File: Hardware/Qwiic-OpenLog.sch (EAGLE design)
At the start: 40 parts, among them J1 MICRO-SD, J10 GATORGATOR_MINI, J2 GATORGATOR_MINI, J3 GATORGATOR_MINI, J4 GATORGATOR_MINI, J5 ISP, J6 GATORGATOR_MINI, J7 GATORGATOR_MINI, J8 GATORGATOR_MINI, J9 GATORGATOR_MINI, Q1 16MHZ, U1 RV-1805, U2 ATMEGA328P

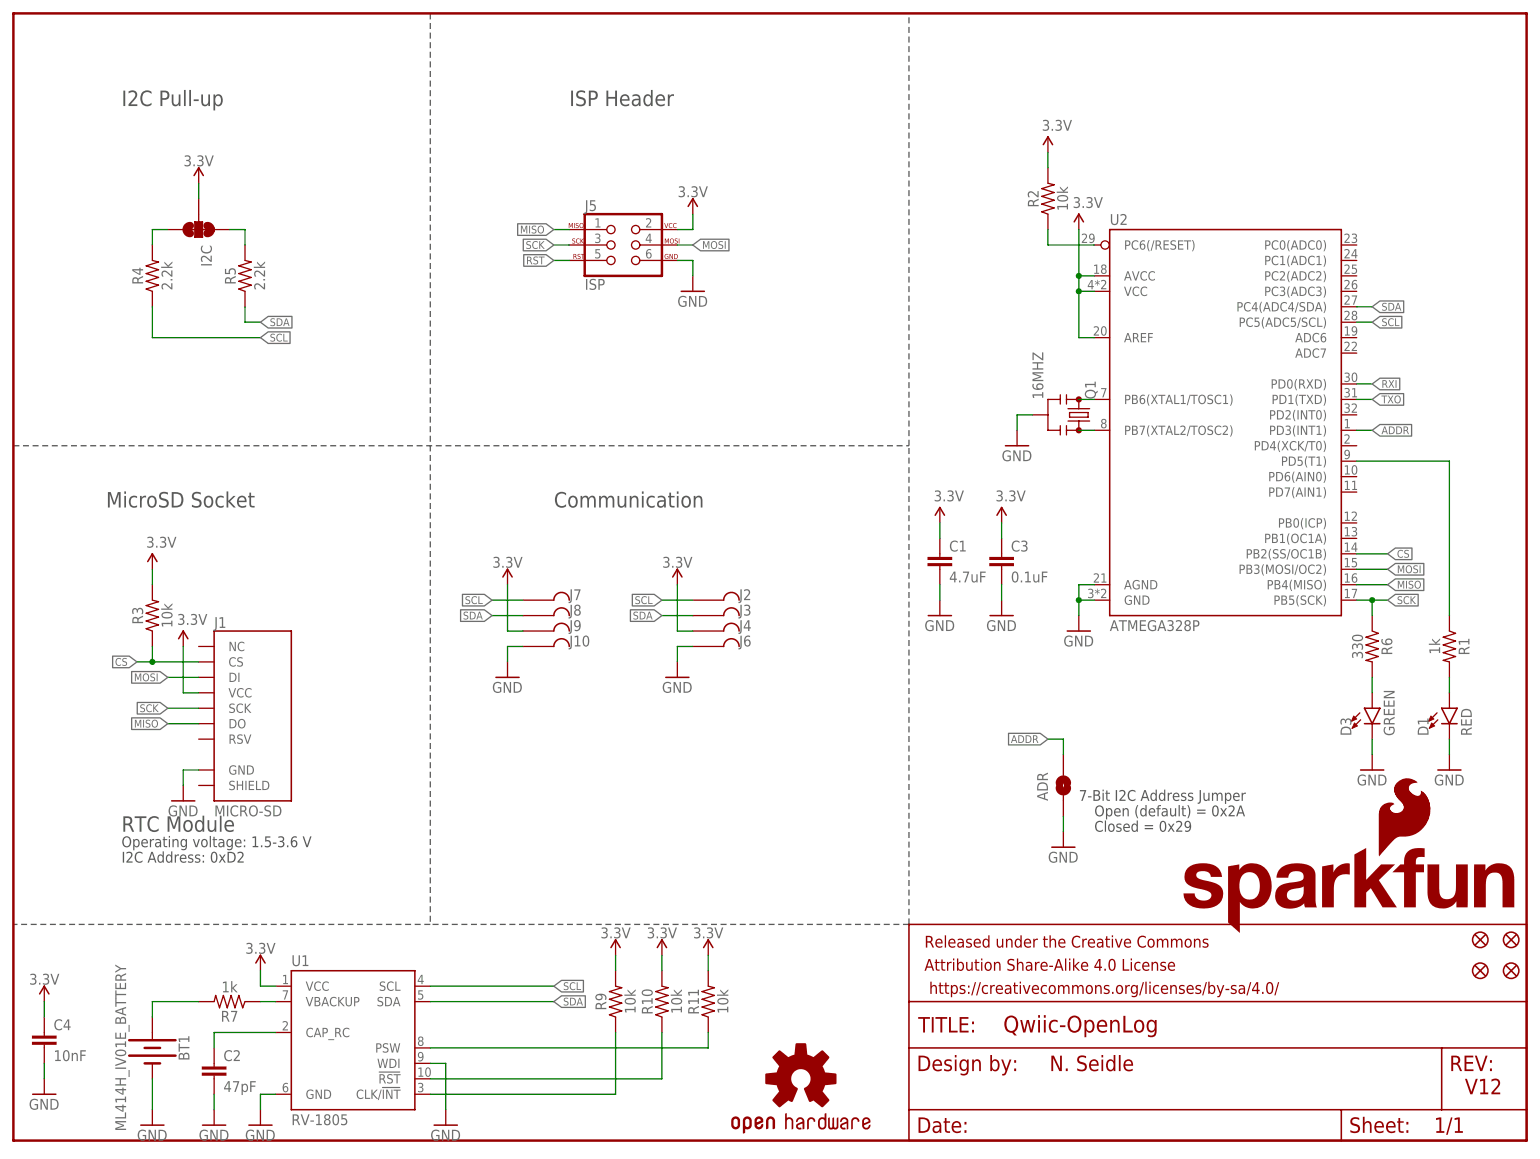
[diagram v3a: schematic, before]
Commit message: updating silk
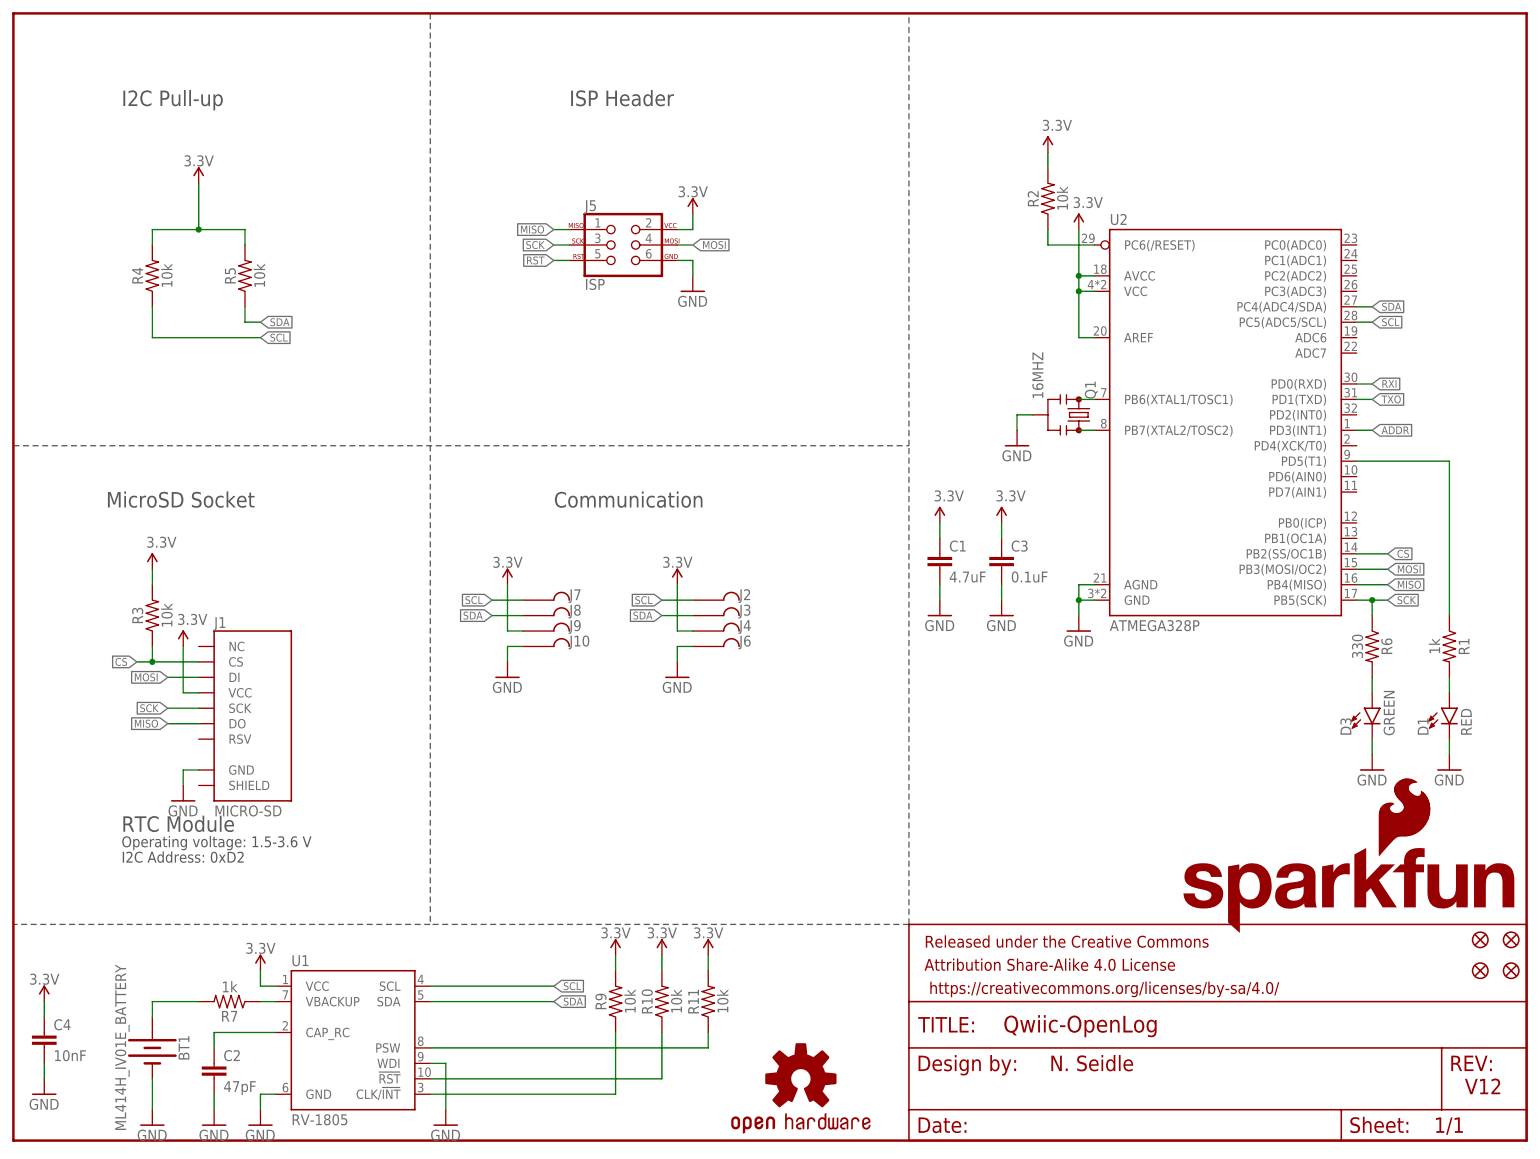
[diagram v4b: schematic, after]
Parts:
- removed ADR: SOLDERJUMPERNO, SparkFun:SOLDERJUMPERNO
- removed I2C: JUMPER-SMT_3_2-NC_TRACE_SILK, SparkFun-Jumpers:JUMPER-SMT_3_2-NC_TRACE_SILK
- R4, R5: value 2.2k -> 10k; device SparkFun-Resistors:2.2KOHM-0603-1/10W-1% -> SparkFun-Resistors:10KOHM-0603-1/10W-1%
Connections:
- removed net N$5: I2C.1, R5.2
- removed net N$6: I2C.3, R4.2
- net 3.3V: now also R4.2, R5.2; no longer I2C.2
- net ADDR: no longer ADR.2
- net GND: no longer ADR.1
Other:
- note removed: "7-Bit I2C Address Jumper"
- note removed: "Closed = 0x29"
- note removed: "Open (default) = 0x2A"
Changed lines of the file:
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@@
 <?xml version="1.0" encoding="utf-8"?>
 <!DOCTYPE eagle SYSTEM "eagle.dtd">
-<eagle version="9.3.1">
+<eagle version="9.1.0">
 <drawing>
 <settings>
@@
 <part name="P+3" library="SparkFun" deviceset="3.3V" device=""/>
 <part name="GND7" library="SparkFun" deviceset="GND" device=""/>
-<part name="GND10" library="SparkFun" deviceset="GND" device=""/>
-<part name="ADR" library="SparkFun" deviceset="SOLDERJUMPER" device="NO" value=""/>
-<part name="R4" library="SparkFun-Resistors" deviceset="2.2KOHM" device="-0603-1/10W-1%" value="2.2k"/>
-<part name="R5" library="SparkFun-Resistors" deviceset="2.2KOHM" device="-0603-1/10W-1%" value="2.2k"/>
-<part name="I2C" library="SparkFun-Jumpers" deviceset="JUMPER-SMT_3_2-NC_TRACE" device="_SILK" value=""/>
+<part name="R4" library="SparkFun-Resistors" deviceset="10KOHM" device="-0603-1/10W-1%" value="10k"/>
+<part name="R5" library="SparkFun-Resistors" deviceset="10KOHM" device="-0603-1/10W-1%" value="10k"/>
 <part name="SUPPLY1" library="SparkFun-PowerSymbols" deviceset="3.3V" device=""/>
 <part name="J5" library="SparkFun-Connectors" deviceset="AVR_SPI_PROG_3X2" device="TESTPOINTS" value="ISP"/>
@@
 <wire x1="0" y1="114.3" x2="147.32" y2="114.3" width="0.2032" layer="97" style="shortdash"/>
 <wire x1="68.58" y1="185.42" x2="68.58" y2="35.56" width="0.2032" layer="97" style="shortdash"/>
-<text x="175.26" y="55.88" size="1.778" layer="97">7-Bit I2C Address Jumper</text>
-<text x="177.8" y="50.8" size="1.778" layer="97">Closed = 0x29</text>
-<text x="177.8" y="53.34" size="1.778" layer="97">Open (default) = 0x2A</text>
 <text x="17.78" y="50.8" size="2.54" layer="97" font="vector">RTC Module</text>
 <text x="17.78" y="48.26" size="1.778" layer="97">Operating voltage: 1.5-3.6 V</text>
@@
 <attribute name="VALUE" x="149.86" y="83.82" size="1.778" layer="96"/>
 </instance>
-<instance part="GND10" gate="1" x="172.72" y="48.26" smashed="yes">
-<attribute name="VALUE" x="170.18" y="45.72" size="1.778" layer="96"/>
-</instance>
-<instance part="ADR" gate="1" x="172.72" y="58.42" smashed="yes" rot="R90">
-<attribute name="NAME" x="170.18" y="55.88" size="1.778" layer="95" rot="R90"/>
-<attribute name="VALUE" x="177.8" y="55.88" size="1.778" layer="96" rot="R90"/>
-</instance>
 <instance part="R4" gate="G$1" x="22.86" y="142.24" smashed="yes" rot="R90">
 <attribute name="NAME" x="21.336" y="142.24" size="1.778" layer="95" font="vector" rot="R90" align="bottom-center"/>
@@
 <attribute name="NAME" x="36.576" y="142.24" size="1.778" layer="95" font="vector" rot="R90" align="bottom-center"/>
 <attribute name="VALUE" x="39.624" y="142.24" size="1.778" layer="96" font="vector" rot="R90" align="top-center"/>
-</instance>
-<instance part="I2C" gate="G$1" x="30.48" y="149.86" smashed="yes" rot="R270">
-<attribute name="NAME" x="30.861" y="147.32" size="1.778" layer="95" font="vector" rot="R270"/>
-<attribute name="VALUE" x="30.099" y="147.32" size="1.778" layer="96" font="vector" rot="R270" align="top-left"/>
 </instance>
 <instance part="SUPPLY1" gate="G$1" x="30.48" y="157.48" smashed="yes">
@@
 <pinref part="GND7" gate="1" pin="GND"/>
 <wire x1="152.4" y1="88.9" x2="152.4" y2="91.44" width="0.1524" layer="91"/>
-</segment>
-<segment>
-<wire x1="172.72" y1="50.8" x2="172.72" y2="53.34" width="0.1524" layer="91"/>
-<pinref part="GND10" gate="1" pin="GND"/>
-<pinref part="ADR" gate="1" pin="1"/>
 </segment>
 <segment>
@@
 </segment>
 <segment>
-<pinref part="I2C" gate="G$1" pin="2"/>
-<wire x1="30.48" y1="157.48" x2="30.48" y2="154.94" width="0.1524" layer="91"/>
 <pinref part="SUPPLY1" gate="G$1" pin="3.3V"/>
+<pinref part="R4" gate="G$1" pin="2"/>
+<wire x1="22.86" y1="147.32" x2="22.86" y2="149.86" width="0.1524" layer="91"/>
+<pinref part="R5" gate="G$1" pin="2"/>
+<wire x1="38.1" y1="147.32" x2="38.1" y2="149.86" width="0.1524" layer="91"/>
+<wire x1="22.86" y1="149.86" x2="30.48" y2="149.86" width="0.1524" layer="91"/>
+<wire x1="30.48" y1="149.86" x2="38.1" y2="149.86" width="0.1524" layer="91"/>
+<wire x1="30.48" y1="157.48" x2="30.48" y2="149.86" width="0.1524" layer="91"/>
+<junction x="30.48" y="149.86"/>
 </segment>
 <segment>
@@
 <net name="ADDR" class="0">
 <segment>
-<wire x1="172.72" y1="63.5" x2="172.72" y2="66.04" width="0.1524" layer="91"/>
-<pinref part="ADR" gate="1" pin="2"/>
-<wire x1="170.18" y1="66.04" x2="172.72" y2="66.04" width="0.1524" layer="91"/>
-<label x="170.18" y="66.04" size="1.27" layer="95" rot="R180" xref="yes"/>
-</segment>
-<segment>
 <wire x1="220.98" y1="116.84" x2="223.52" y2="116.84" width="0.1524" layer="91"/>
 <label x="223.52" y="116.84" size="1.27" layer="95" xref="yes"/>
@@
 </segment>
 </net>
-<net name="N$5" class="0">
-<segment>
-<pinref part="R5" gate="G$1" pin="2"/>
-<wire x1="38.1" y1="147.32" x2="38.1" y2="149.86" width="0.1524" layer="91"/>
-<pinref part="I2C" gate="G$1" pin="1"/>
-<wire x1="38.1" y1="149.86" x2="35.56" y2="149.86" width="0.1524" layer="91"/>
-</segment>
-</net>
-<net name="N$6" class="0">
-<segment>
-<pinref part="R4" gate="G$1" pin="2"/>
-<wire x1="22.86" y1="147.32" x2="22.86" y2="149.86" width="0.1524" layer="91"/>
-<pinref part="I2C" gate="G$1" pin="3"/>
-<wire x1="22.86" y1="149.86" x2="25.4" y2="149.86" width="0.1524" layer="91"/>
-</segment>
-</net>

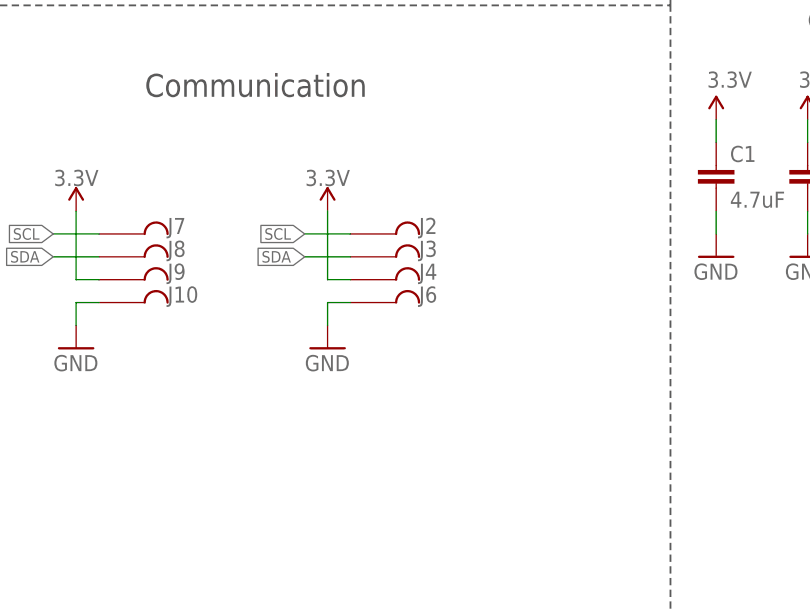
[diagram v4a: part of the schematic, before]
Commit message: adding protection circuitry
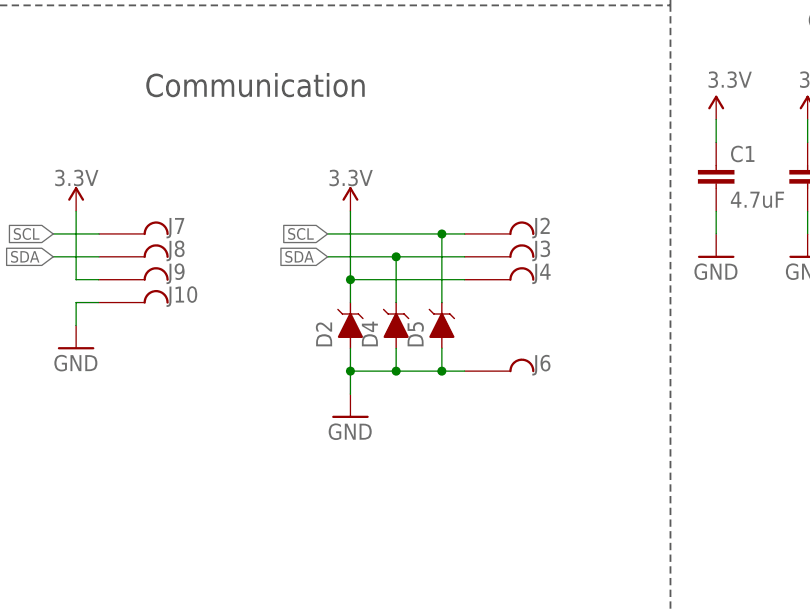
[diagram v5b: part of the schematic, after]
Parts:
- added D2, D4, D5: 3.6V, SparkFun-DiscreteSemi:DIODE-ZENER-BZT52C3V6S
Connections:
- net 3.3V: now also D2.C
- net GND: now also D2.A, D4.A, D5.A
- net SCL: now also D5.C
- net SDA: now also D4.C
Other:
- moved on the sheet: J2, J3, J4, J6
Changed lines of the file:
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@@
 <?xml version="1.0" encoding="utf-8"?>
 <!DOCTYPE eagle SYSTEM "eagle.dtd">
-<eagle version="9.1.0">
+<eagle version="9.3.1">
 <drawing>
 <settings>
@@
 <part name="R7" library="SparkFun-Resistors" deviceset="1KOHM" device="-0603-1/10W-1%" value="1k"/>
 <part name="GND16" library="SparkFun" deviceset="GND" device=""/>
+<part name="D2" library="SparkFun-DiscreteSemi" deviceset="DIODE-ZENER" device="-BZT52C3V6S" value="3.6V"/>
+<part name="D4" library="SparkFun-DiscreteSemi" deviceset="DIODE-ZENER" device="-BZT52C3V6S" value="3.6V"/>
+<part name="D5" library="SparkFun-DiscreteSemi" deviceset="DIODE-ZENER" device="-BZT52C3V6S" value="3.6V"/>
 </parts>
 <sheets>
@@
 <attribute name="NAME" x="91.44" y="81.28" size="1.778" layer="95" font="vector"/>
 </instance>
-<instance part="SUPPLY3" gate="G$1" x="109.22" y="91.44" smashed="yes">
-<attribute name="VALUE" x="109.22" y="94.234" size="1.778" layer="96" align="bottom-center"/>
-</instance>
-<instance part="GND6" gate="1" x="109.22" y="76.2" smashed="yes">
-<attribute name="VALUE" x="106.68" y="73.66" size="1.778" layer="96"/>
-</instance>
-<instance part="J2" gate="G$1" x="114.3" y="88.9" smashed="yes">
-<attribute name="NAME" x="119.38" y="88.9" size="1.778" layer="95" font="vector"/>
-</instance>
-<instance part="J3" gate="G$1" x="114.3" y="86.36" smashed="yes">
-<attribute name="NAME" x="119.38" y="86.36" size="1.778" layer="95" font="vector"/>
-</instance>
-<instance part="J4" gate="G$1" x="114.3" y="83.82" smashed="yes">
-<attribute name="NAME" x="119.38" y="83.82" size="1.778" layer="95" font="vector"/>
-</instance>
-<instance part="J6" gate="G$1" x="114.3" y="81.28" smashed="yes">
-<attribute name="NAME" x="119.38" y="81.28" size="1.778" layer="95" font="vector"/>
+<instance part="SUPPLY3" gate="G$1" x="111.76" y="91.44" smashed="yes">
+<attribute name="VALUE" x="111.76" y="94.234" size="1.778" layer="96" align="bottom-center"/>
+</instance>
+<instance part="GND6" gate="1" x="111.76" y="68.58" smashed="yes">
+<attribute name="VALUE" x="109.22" y="66.04" size="1.778" layer="96"/>
+</instance>
+<instance part="J2" gate="G$1" x="127" y="88.9" smashed="yes">
+<attribute name="NAME" x="132.08" y="88.9" size="1.778" layer="95" font="vector"/>
+</instance>
+<instance part="J3" gate="G$1" x="127" y="86.36" smashed="yes">
+<attribute name="NAME" x="132.08" y="86.36" size="1.778" layer="95" font="vector"/>
+</instance>
+<instance part="J4" gate="G$1" x="127" y="83.82" smashed="yes">
+<attribute name="NAME" x="132.08" y="83.82" size="1.778" layer="95" font="vector"/>
+</instance>
+<instance part="J6" gate="G$1" x="127" y="73.66" smashed="yes">
+<attribute name="NAME" x="132.08" y="73.66" size="1.778" layer="95" font="vector"/>
 </instance>
 <instance part="R9" gate="G$1" x="99.06" y="22.86" smashed="yes" rot="R90">
@@
 <instance part="GND16" gate="1" x="22.86" y="2.54" smashed="yes">
 <attribute name="VALUE" x="20.32" y="0" size="1.778" layer="96"/>
+</instance>
+<instance part="D2" gate="G$1" x="111.76" y="78.74" smashed="yes" rot="R90">
+<attribute name="NAME" x="109.728" y="76.2" size="1.778" layer="95" font="vector" rot="R90"/>
+</instance>
+<instance part="D4" gate="G$1" x="116.84" y="78.74" smashed="yes" rot="R90">
+<attribute name="NAME" x="114.808" y="76.2" size="1.778" layer="95" font="vector" rot="R90"/>
+</instance>
+<instance part="D5" gate="G$1" x="121.92" y="78.74" smashed="yes" rot="R90">
+<attribute name="NAME" x="119.888" y="76.2" size="1.778" layer="95" font="vector" rot="R90"/>
 </instance>
 </instances>
@@
 </segment>
 <segment>
-<wire x1="111.76" y1="81.28" x2="109.22" y2="81.28" width="0.1524" layer="91"/>
-<wire x1="109.22" y1="81.28" x2="109.22" y2="78.74" width="0.1524" layer="91"/>
+<wire x1="124.46" y1="73.66" x2="121.92" y2="73.66" width="0.1524" layer="91"/>
+<wire x1="121.92" y1="73.66" x2="116.84" y2="73.66" width="0.1524" layer="91"/>
+<wire x1="116.84" y1="73.66" x2="111.76" y2="73.66" width="0.1524" layer="91"/>
+<wire x1="111.76" y1="73.66" x2="111.76" y2="71.12" width="0.1524" layer="91"/>
 <pinref part="GND6" gate="1" pin="GND"/>
 <pinref part="J6" gate="G$1" pin="P$1"/>
+<pinref part="D5" gate="G$1" pin="A"/>
+<wire x1="121.92" y1="76.2" x2="121.92" y2="73.66" width="0.1524" layer="91"/>
+<junction x="121.92" y="73.66"/>
+<pinref part="D4" gate="G$1" pin="A"/>
+<wire x1="116.84" y1="76.2" x2="116.84" y2="73.66" width="0.1524" layer="91"/>
+<junction x="116.84" y="73.66"/>
+<pinref part="D2" gate="G$1" pin="A"/>
+<wire x1="111.76" y1="76.2" x2="111.76" y2="73.66" width="0.1524" layer="91"/>
+<junction x="111.76" y="73.66"/>
 </segment>
 <segment>
@@
 </segment>
 <segment>
-<wire x1="111.76" y1="83.82" x2="109.22" y2="83.82" width="0.1524" layer="91"/>
-<wire x1="109.22" y1="83.82" x2="109.22" y2="91.44" width="0.1524" layer="91"/>
+<wire x1="124.46" y1="83.82" x2="111.76" y2="83.82" width="0.1524" layer="91"/>
+<wire x1="111.76" y1="83.82" x2="111.76" y2="91.44" width="0.1524" layer="91"/>
 <pinref part="SUPPLY3" gate="G$1" pin="3.3V"/>
 <pinref part="J4" gate="G$1" pin="P$1"/>
+<pinref part="D2" gate="G$1" pin="C"/>
+<wire x1="111.76" y1="83.82" x2="111.76" y2="81.28" width="0.1524" layer="91"/>
+<junction x="111.76" y="83.82"/>
 </segment>
 <segment>
@@
 </segment>
 <segment>
-<wire x1="111.76" y1="88.9" x2="106.68" y2="88.9" width="0.1524" layer="91"/>
-<label x="106.68" y="88.9" size="1.27" layer="95" rot="R180" xref="yes"/>
+<label x="109.22" y="88.9" size="1.27" layer="95" rot="R180" xref="yes"/>
 <pinref part="J2" gate="G$1" pin="P$1"/>
+<wire x1="124.46" y1="88.9" x2="121.92" y2="88.9" width="0.1524" layer="91"/>
+<pinref part="D5" gate="G$1" pin="C"/>
+<wire x1="121.92" y1="88.9" x2="109.22" y2="88.9" width="0.1524" layer="91"/>
+<wire x1="121.92" y1="88.9" x2="121.92" y2="81.28" width="0.1524" layer="91"/>
+<junction x="121.92" y="88.9"/>
 </segment>
 <segment>
@@
 </segment>
 <segment>
-<wire x1="111.76" y1="86.36" x2="106.68" y2="86.36" width="0.1524" layer="91"/>
-<label x="106.68" y="86.36" size="1.27" layer="95" rot="R180" xref="yes"/>
+<label x="109.22" y="86.36" size="1.27" layer="95" rot="R180" xref="yes"/>
 <pinref part="J3" gate="G$1" pin="P$1"/>
-</segment>
-<segment>
+<wire x1="124.46" y1="86.36" x2="116.84" y2="86.36" width="0.1524" layer="91"/>
+<pinref part="D4" gate="G$1" pin="C"/>
+<wire x1="116.84" y1="86.36" x2="109.22" y2="86.36" width="0.1524" layer="91"/>
+<wire x1="116.84" y1="86.36" x2="116.84" y2="81.28" width="0.1524" layer="91"/>
+<junction x="116.84" y="86.36"/>
+</segment>
+<segment>

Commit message: finalizing silk and schematic before design review
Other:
- note added: "A. England"
- note added: "v01"
- note removed: "N. Seidle"
- note removed: "V12"
- moved on the sheet: BT1, C2, C4, D2, D4, D5, J1, J10, J2, J3, J4, J6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

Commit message: engineer run of checklist
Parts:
- added Q2: 2.5A/30V/105mΩ, SparkFun-DiscreteSemi:MOSFET_PCH-DMG2307L
- added R8: 10k, SparkFun-Resistors:10KOHM-0603-1/10W-1%
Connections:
- new net N$5: J4.P$1, J9.P$1, Q2.D
- new net N$6: D2.A, Q2.G, R8.2
- net 3.3V: now also Q2.S; no longer J4.P$1, J9.P$1
- net GND: now also R8.1; no longer D2.A
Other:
- note added: "ATMEGA328"
- moved on the sheet: D2, D4, D5, J2, J3, J4, J6, J9, R10, R11, R9
